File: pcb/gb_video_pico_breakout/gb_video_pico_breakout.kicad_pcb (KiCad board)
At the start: 11 copper layers, 44 x 73 mm, 19 parts, among them J1 Conn_01x05, U1 SN74LVC1G17QDCKRQ1, U2 SN74LVC1G17QDCKRQ1, U3 SN74LVC1G17QDCKRQ1

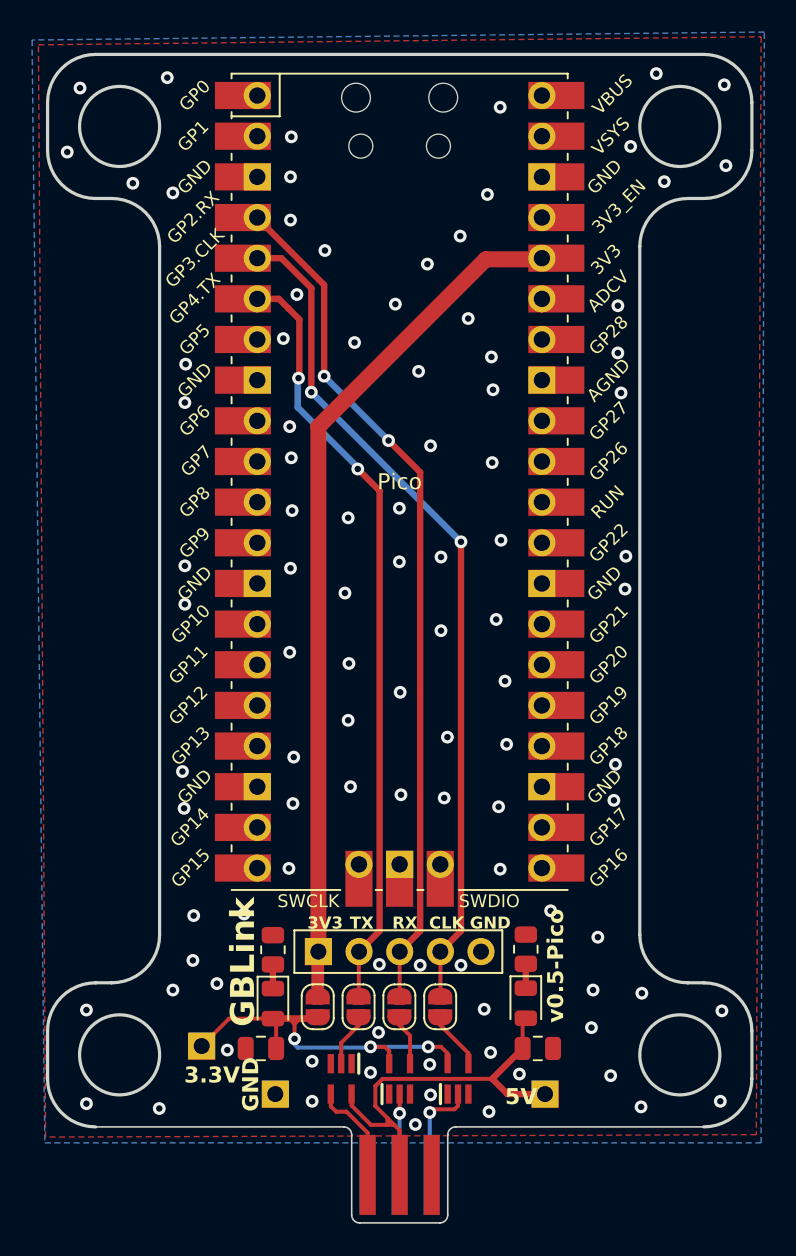
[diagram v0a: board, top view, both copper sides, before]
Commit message: add serialtransfer support
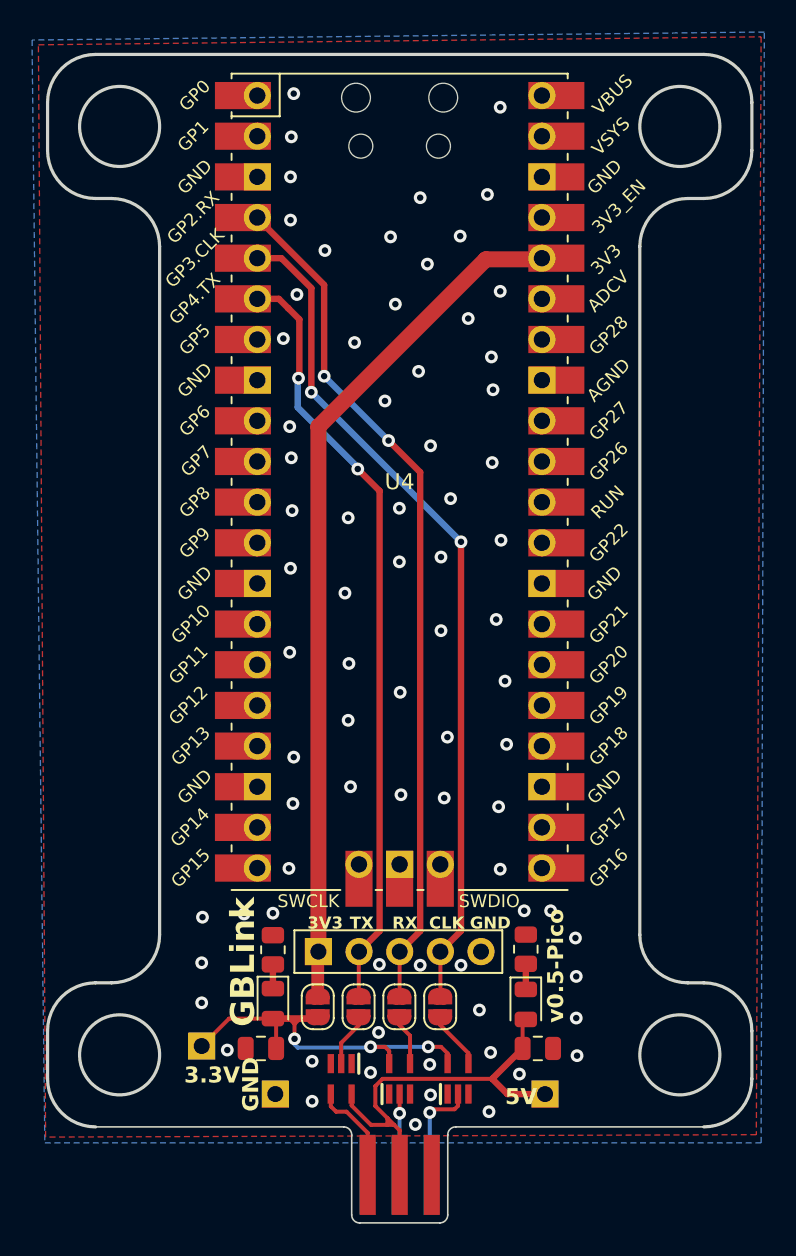
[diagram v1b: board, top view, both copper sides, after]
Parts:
- moved D1 0.07 mm to (157.8, 115.3)
- renumbered Pico to U4
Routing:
- net GND: vias 100 -> 77
